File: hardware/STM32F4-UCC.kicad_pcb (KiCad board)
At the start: 2 copper layers, 111.1 x 60.7 mm, 121 parts, among them J1 DB15, J2 STM32F4_Discovery_Header, J3 RJ45-TRANSFO_W, Q1 IRLML6402, SW1 PE4, SW2 PE5, SW3 PE6, SW4 PE2, U1 RGB, U2 FT230X, U3 DP83848C, U4 MCP1825S-3302E, U5 microSD, X1 50Mhz

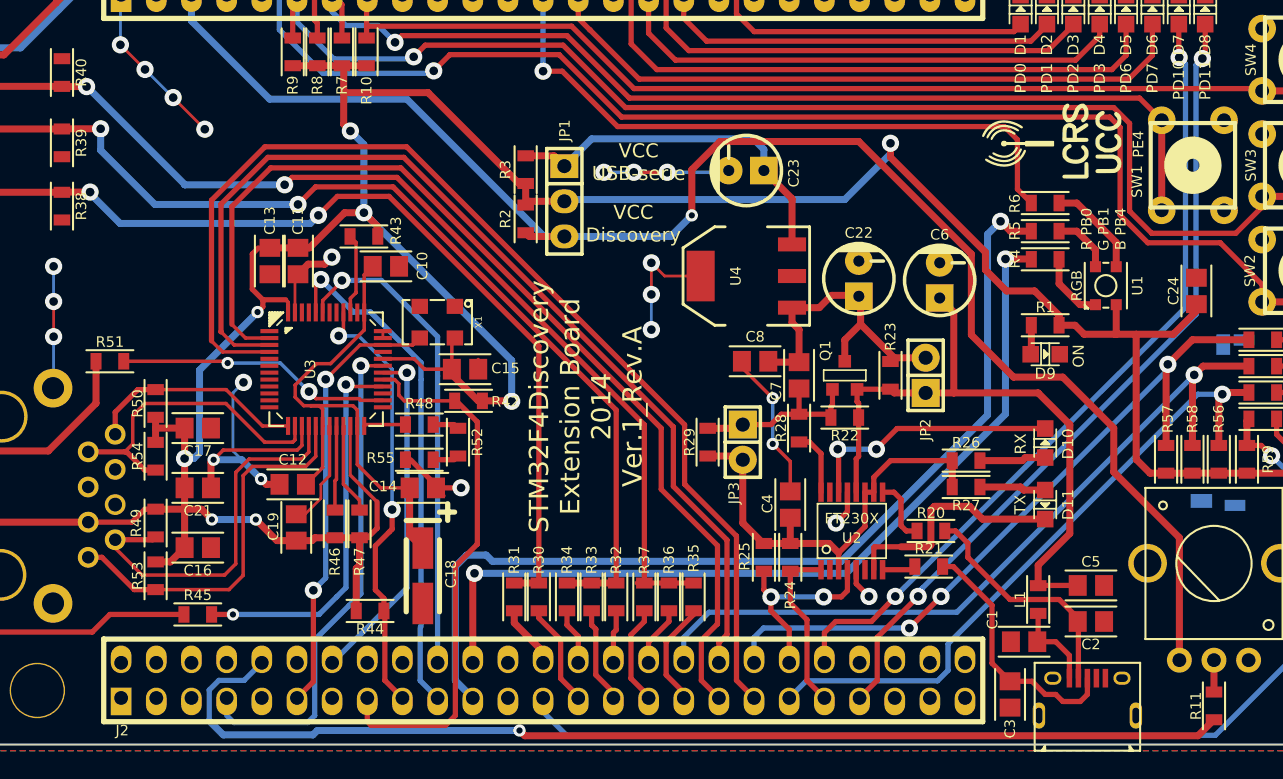
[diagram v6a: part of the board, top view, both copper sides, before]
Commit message: Cambios minimos y nuevo PDF y gerbers
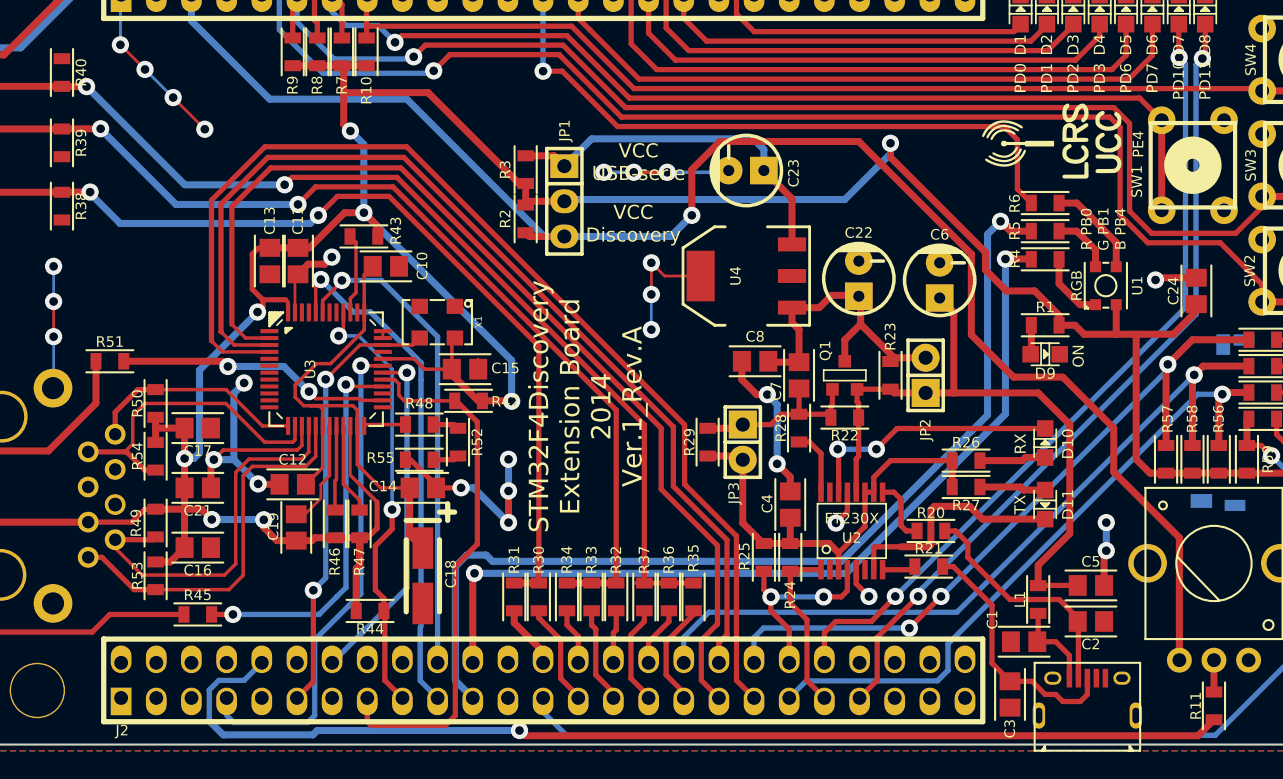
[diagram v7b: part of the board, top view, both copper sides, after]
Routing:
- net GND: track 99.9 -> 115.1 mm, vias 22 -> 28
- net Net-(J1-Pad2): track 74.0 -> 73.1 mm
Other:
- rule via_min_drill: 0.508 -> 0.889
- rule via_min_size: 0.889 -> 1.2446

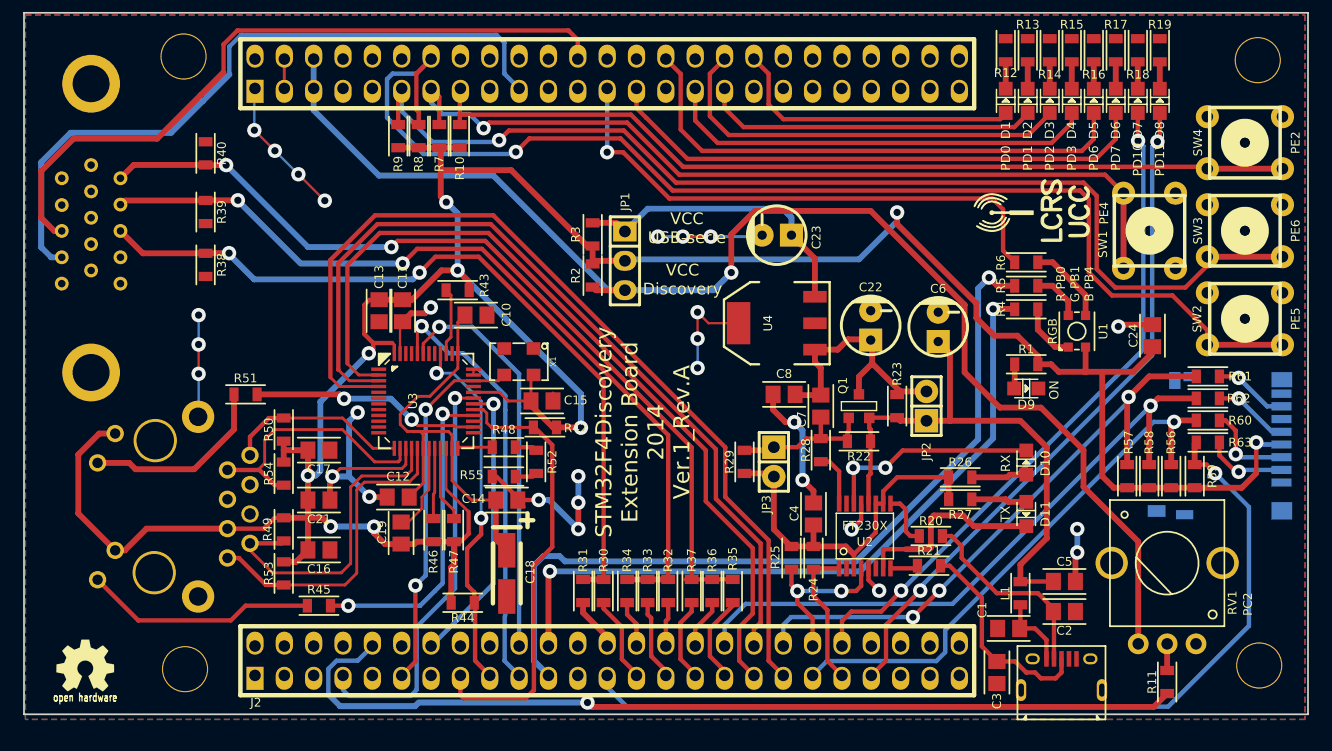
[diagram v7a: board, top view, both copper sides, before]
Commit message: Placa con errores solucionados
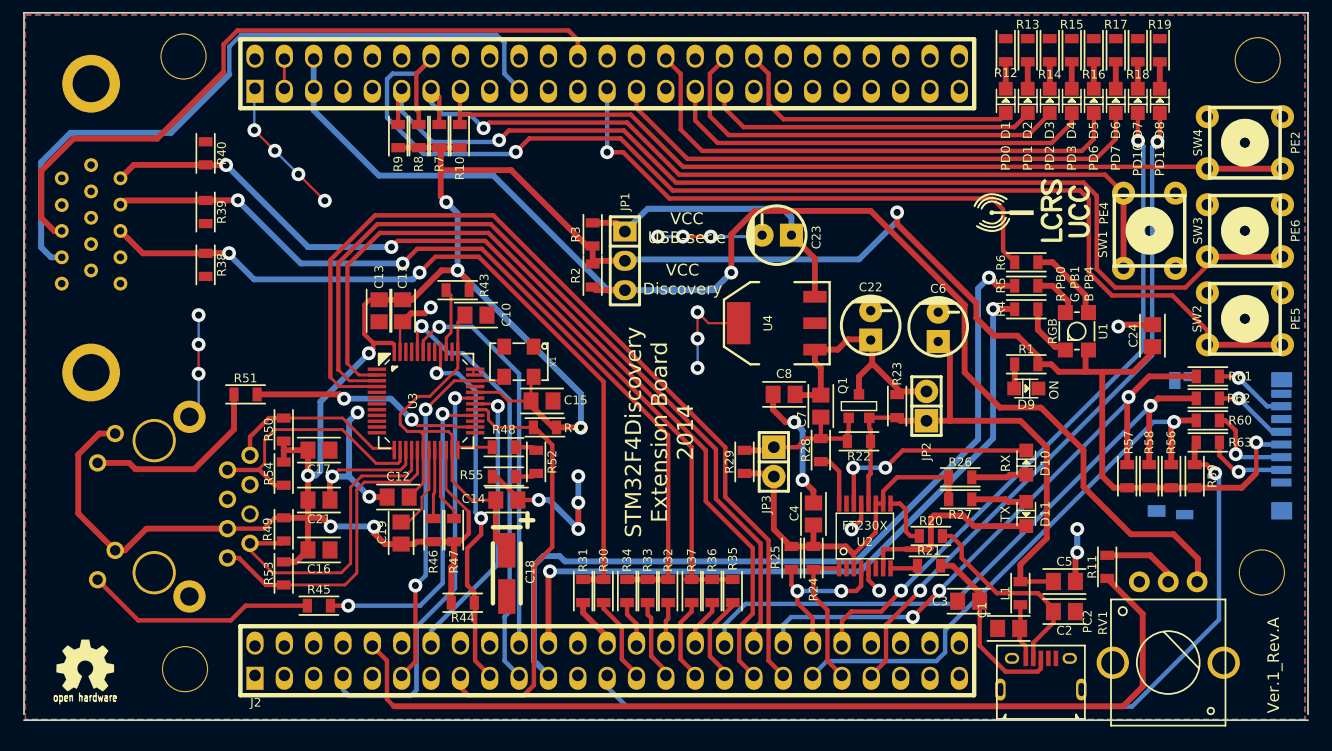
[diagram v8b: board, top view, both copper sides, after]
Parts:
- J3: footprint w_Connectors:RJ45 -> RJ45
- U1: footprint w_Connectors:PLCC4 -> PLCC4
- U3: footprint w_Connectors:lqfp48 -> lqfp48
- X1: footprint w_Connectors:crystal_fa128 -> crystal_fa128
- moved R11 11.2 mm to (186.2, 118.1)
- moved MH 8.06 mm to (199.6, 118.6)
- moved C3 6.63 mm to (174.2, 121.1), turned to 0 degrees
- moved RV1 5.37 mm to (191.5, 119.4), turned to 180 degrees
- moved USB-Serie1 1.78 mm to (180.4, 128.7)
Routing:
- net /SD-Card/Dat3/CS: track 78.6 -> 74.6 mm
- net Net-(R11-Pad2): track 2.30 -> 6.07 mm
- net Net-(C3-Pad1): track 18.3 -> 16.1 mm
- net /3.3V_discovery: track 115.9 -> 114.2 mm
- net Net-(C1-Pad1): track 6.45 -> 4.88 mm
- net /PC2: track 80.6 -> 82.1 mm, vias 1 -> 0
- net /Ethernet/MDIO: track 24.9 -> 26.2 mm
- net /Ethernet/NRST: track 38.9 -> 38.0 mm
- net Net-(C2-Pad1): track 17.2 -> 17.9 mm
- net GND: track 115.1 -> 114.4 mm
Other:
- board size 111.1 x 60.7 mm -> 111.1 x 61.2 mm
- net class Alimentacion: via_dia 1.2446 -> 1.2; via_drill 0.889 -> 0.6
- net class Default: via_dia 1.2446 -> 1.2; via_drill 0.889 -> 0.6
- rule via_min_drill: 0.889 -> 0.6
- rule via_min_size: 1.2446 -> 1.2
- board text added: "STM32F4Discovery Extension Board 2014"
- board text added: "Ver.1_Rev.A"
- board text removed: "STM32F4Discovery Extension Board 2014 Ver.1_Rev.A"
